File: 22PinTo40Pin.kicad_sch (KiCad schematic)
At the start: 2 parts, among them J1 Conn_01x15, J2 Conn_01x22

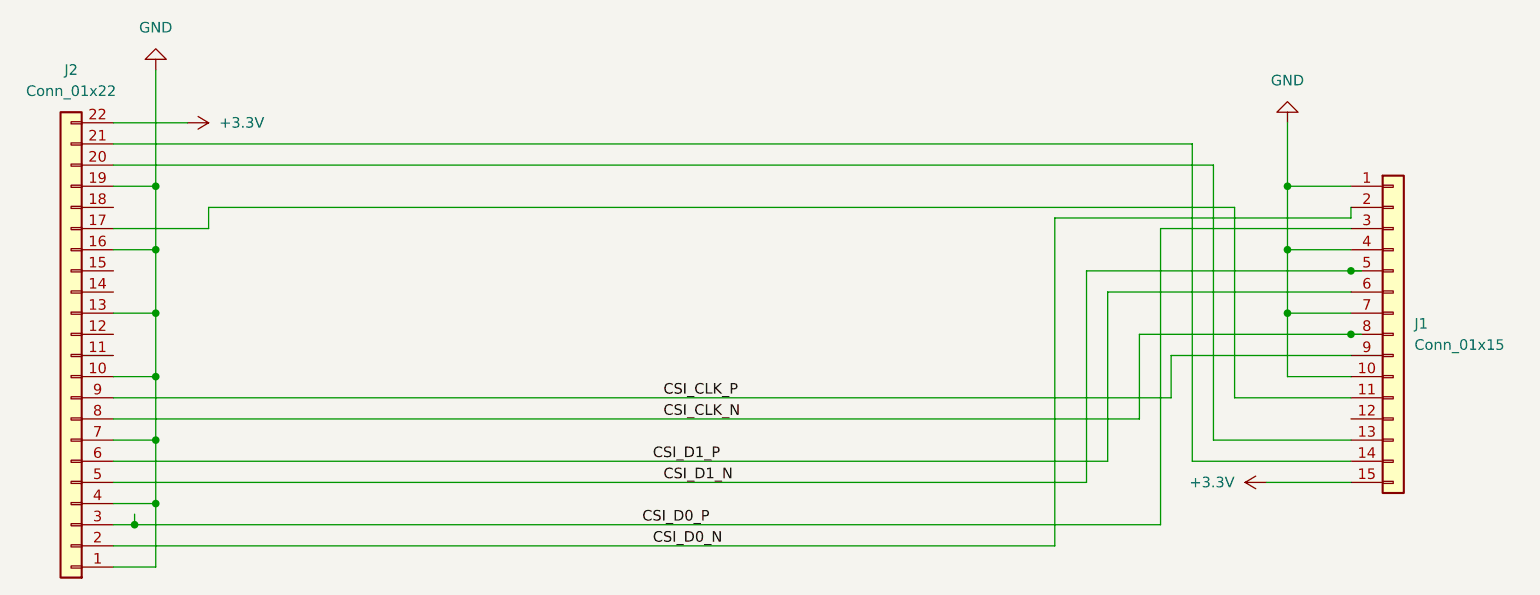
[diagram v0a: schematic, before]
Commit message: fixed lengths, fixed difference between pairs, actually corrected the pinout with 67% confidence of it working ok(hopium)
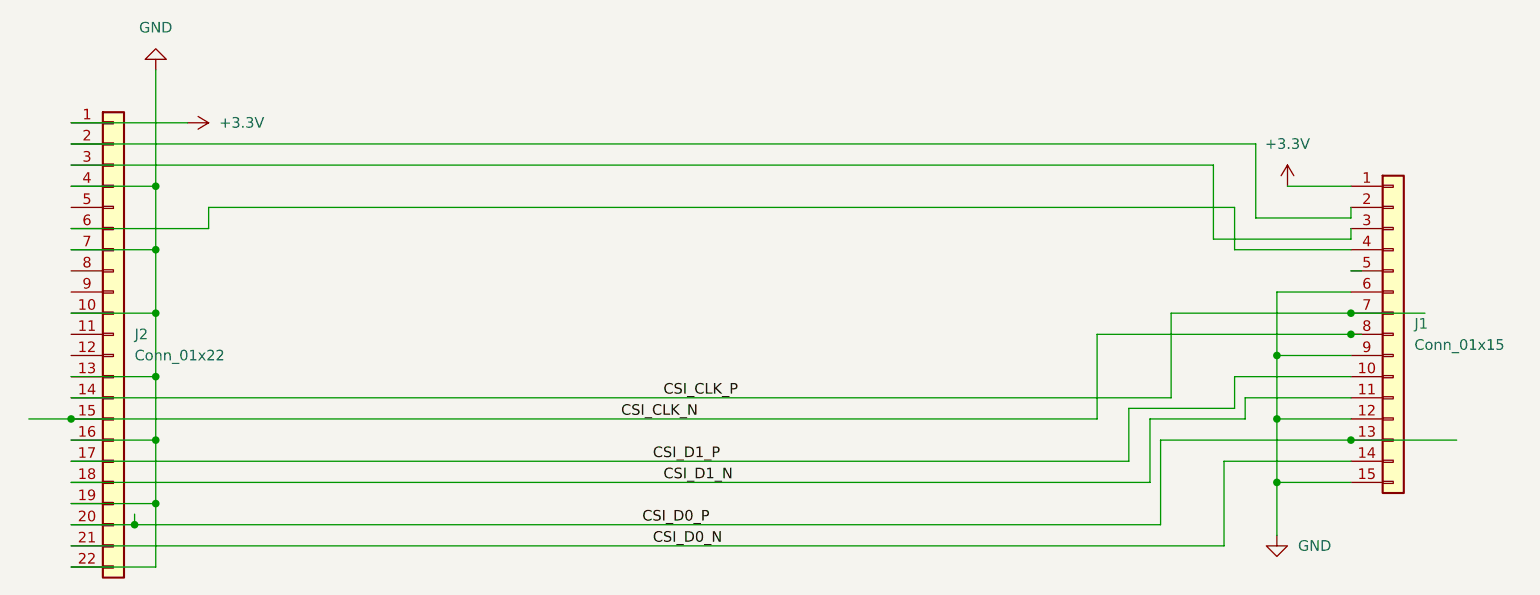
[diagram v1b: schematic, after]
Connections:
- net +3.3V: now also J1.1 (Pin_1), J2.1 (Pin_1); no longer J1.15 (Pin_15), J2.22 (Pin_22)
- net CSI_CLK_N: now also J2.15 (Pin_15); no longer J2.8 (Pin_8)
- net CSI_CLK_P: now also J1.7 (Pin_7), J2.14 (Pin_14); no longer J1.9 (Pin_9), J2.9 (Pin_9)
- net CSI_D0_N: now also J1.14 (Pin_14), J2.21 (Pin_21); no longer J1.2 (Pin_2), J2.2 (Pin_2)
- net CSI_D0_P: now also J1.13 (Pin_13), J2.20 (Pin_20); no longer J1.3 (Pin_3), J2.3 (Pin_3)
- net CSI_D1_N: now also J1.11 (Pin_11), J2.18 (Pin_18); no longer J1.5 (Pin_5), J2.5 (Pin_5)
- net CSI_D1_P: now also J1.10 (Pin_10), J2.17 (Pin_17); no longer J1.6 (Pin_6), J2.6 (Pin_6)
- net GND: now also J1.12 (Pin_12), J1.15 (Pin_15), J1.6 (Pin_6), J1.9 (Pin_9), J2.22 (Pin_22); no longer J1.1 (Pin_1), J1.10 (Pin_10), J1.4 (Pin_4), J1.7 (Pin_7), J2.1 (Pin_1)
- new net: J1.2 (Pin_2), J2.2 (Pin_2)
- new net: J1.3 (Pin_3), J2.3 (Pin_3)
- new net: J1.4 (Pin_4), J2.6 (Pin_6)
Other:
- moved on the sheet: J2
